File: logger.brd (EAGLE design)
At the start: 99 x 44.1 mm, 69 parts, among them IC1 LTC4412, J1 POWER_JACKPTH, Q1 FDN360P, Q2 FDN360P, Q3 2N7002PW, Q4 2N7002PW, U1 FT232RL

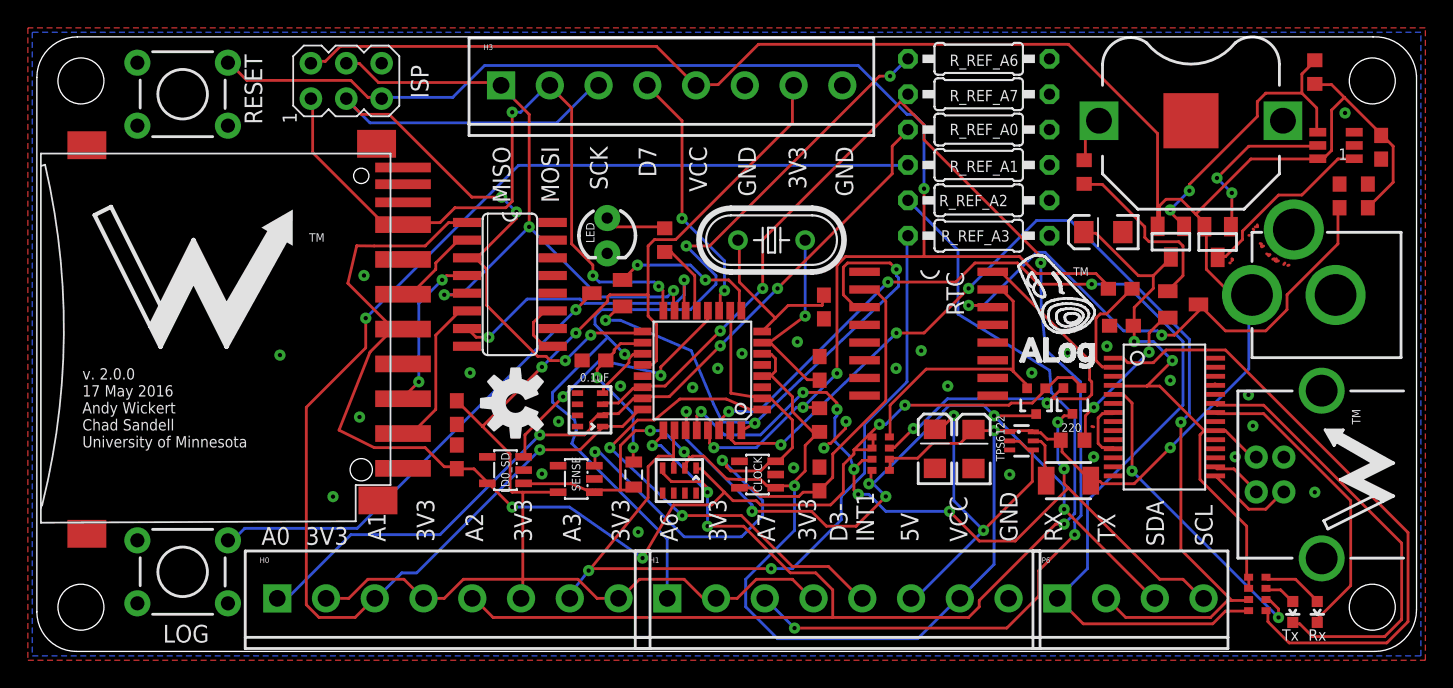
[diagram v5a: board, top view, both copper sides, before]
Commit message: Route EN pin to tie into 3.3V digital pin (D6 I think)
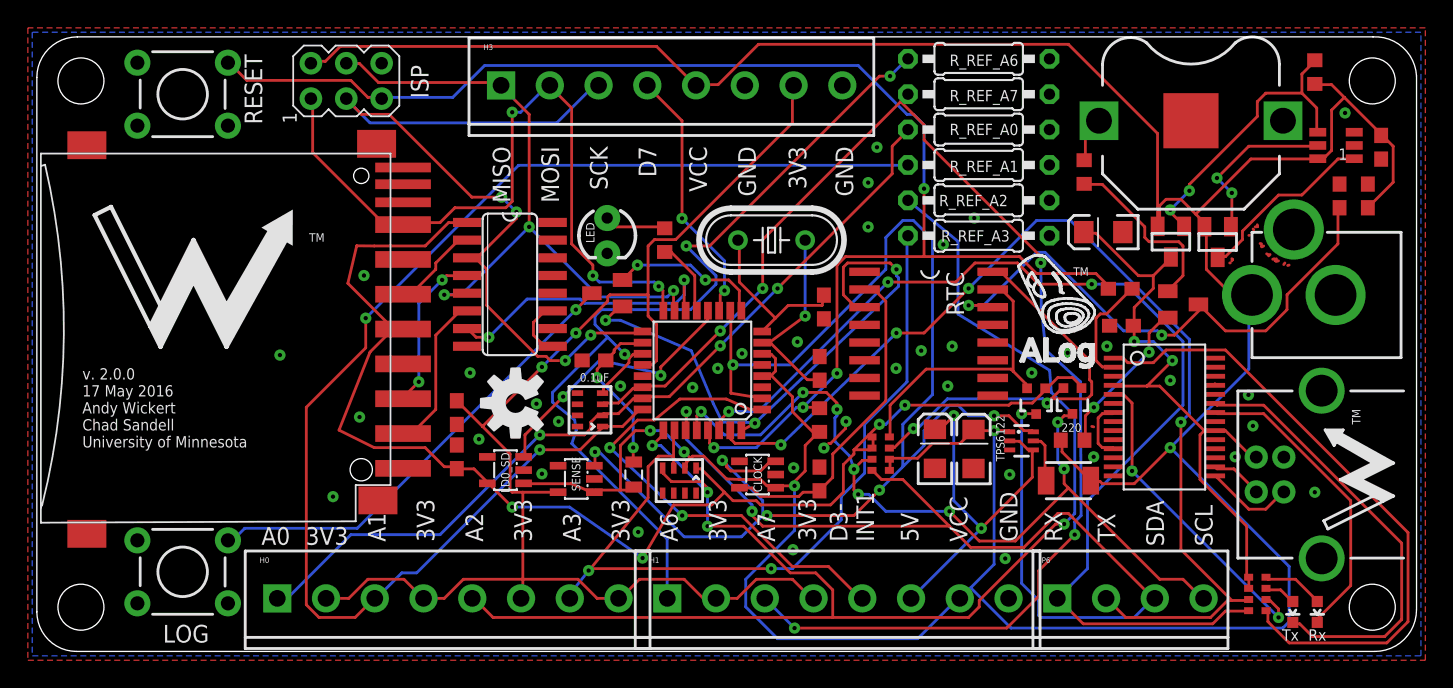
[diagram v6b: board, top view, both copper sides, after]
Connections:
- net D6-CLOCK_3V3_SWITCH: now also TPS6122.6
- net VCC: no longer TPS6122.6
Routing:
- net D6-CLOCK_3V3_SWITCH: track 40.6 -> 96.2 mm, vias 2 -> 6
- net VCC: track 234.9 -> 271.6 mm
- net SDA: track 56.5 -> 76.4 mm, vias 6 -> 3
- net GND: track 13.3 -> 13.4 mm, vias 30 -> 40

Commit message: 5V pin on both sides of board instead of duel ground pins on one side
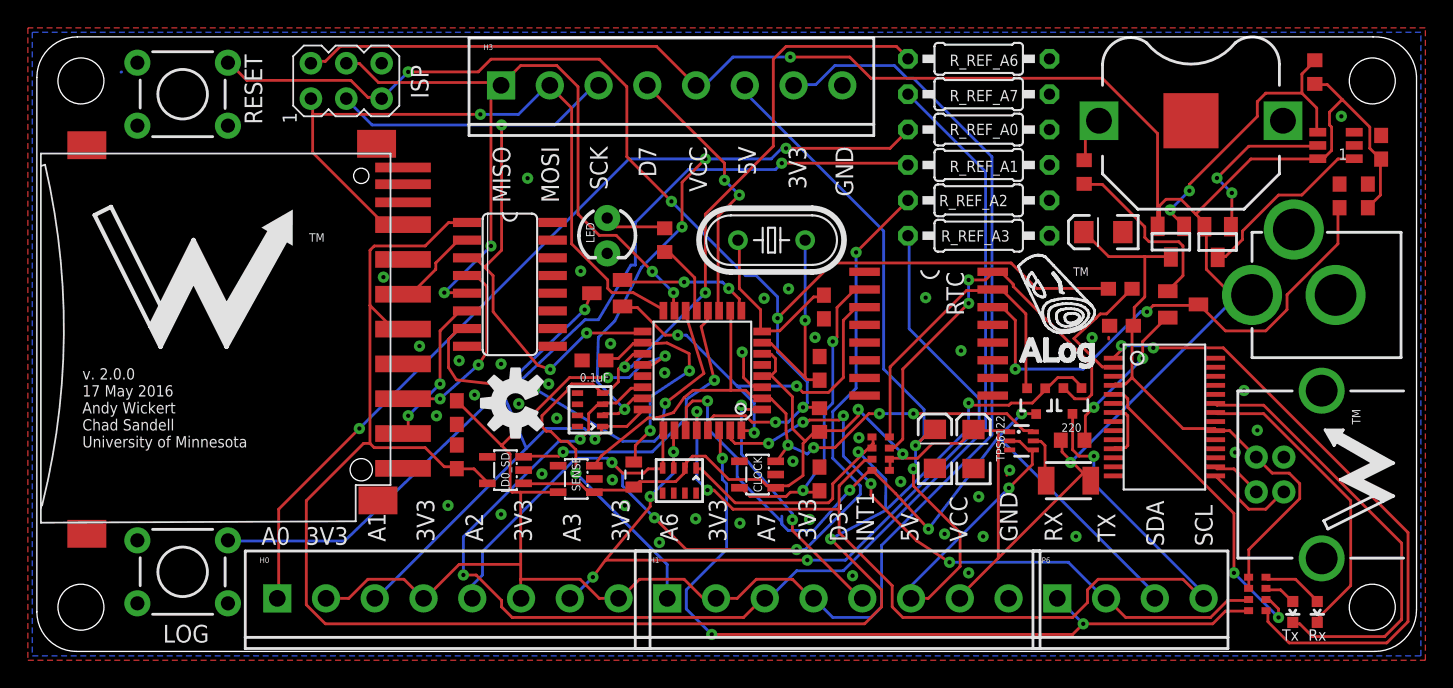
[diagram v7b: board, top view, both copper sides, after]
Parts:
- turned DECOUP to 90 degrees
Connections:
- net 5V: now also H3.6
- net GND: no longer H3.6
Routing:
- net VCC: track 271.6 -> 212.5 mm, vias 5 -> 4
- net D6-CLOCK_3V3_SWITCH: track 96.2 -> 45.7 mm, vias 6 -> 4
- net VDD: track 95.9 -> 143.5 mm, vias 4 -> 3
- net 5V: track 26.9 -> 64.2 mm, vias 2 -> 3
- net +3V3: track 101.1 -> 134.1 mm
- net A2: track 102.1 -> 69.5 mm
- net TX-O: track 75.7 -> 47.1 mm, vias 4 -> 5
- net A1: track 96.6 -> 68.1 mm
- net A0: track 60.7 -> 88.2 mm, vias 3 -> 5
- net RX-I: track 78.1 -> 58.7 mm
- net SDA: track 76.4 -> 57.3 mm, vias 3 -> 4
- net D3-INT1: track 35.0 -> 19.0 mm
- net SCL: track 59.7 -> 73.5 mm, vias 8 -> 3
- net INT0: track 40.9 -> 29.8 mm
- net CS-SD: track 20.7 -> 31.2 mm
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
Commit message: Clock power for pull-ups on I2C
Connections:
- net VCL: now also RN2.5, RN2.6
- net VDD: no longer RN2.5, RN2.6
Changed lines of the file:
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@@
 <contactref element="Q3" pad="1"/>
 <contactref element="Q4" pad="1"/>
-<contactref element="RN2" pad="6"/>
-<contactref element="RN2" pad="5"/>
 <contactref element="C14" pad="A1"/>
 <wire x1="31.3944" y1="13.1064" x2="30.1752" y2="13.1064" width="0.2032" layer="1"/>
@@
 <wire x1="60.0456" y1="15.3924" x2="60.0456" y2="14.9352" width="0.2032" layer="1"/>
 <wire x1="60.0456" y1="14.9352" x2="60.0456" y2="14.6304" width="0.2032" layer="1"/>
-<wire x1="60.0456" y1="14.6304" x2="59.9667" y2="14.5986" width="0.2032" layer="1"/>
-<wire x1="60.0456" y1="15.3924" x2="59.9667" y2="15.3986" width="0.2032" layer="1"/>
 <wire x1="47.7012" y1="13.1064" x2="47.3964" y2="13.1064" width="0.2032" layer="1"/>
 <wire x1="50.1396" y1="10.668" x2="47.7012" y2="13.1064" width="0.2032" layer="1"/>
@@
 <via x="57.15" y="22.2504" extent="1-16" drill="0.3048"/>
 <via x="55.0164" y="11.557" extent="1-16" drill="0.3048"/>
+<contactref element="RN2" pad="6"/>
+<contactref element="RN2" pad="5"/>
+<wire x1="59.9667" y1="14.5986" x2="59.9667" y2="15.3986" width="0" layer="19" extent="1-1"/>
+<wire x1="56.5404" y1="13.716" x2="59.9667" y2="14.5986" width="0" layer="19" extent="1-16"/>
 </signal>
 <signal name="N$12">
